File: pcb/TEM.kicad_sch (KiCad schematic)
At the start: 23 parts, among them J1 Conn_01x04_Pin, SW1 SW_Wuerth_450301014042, U1 AT24CM02-SSHM, U2 AT24CM02-SSHM

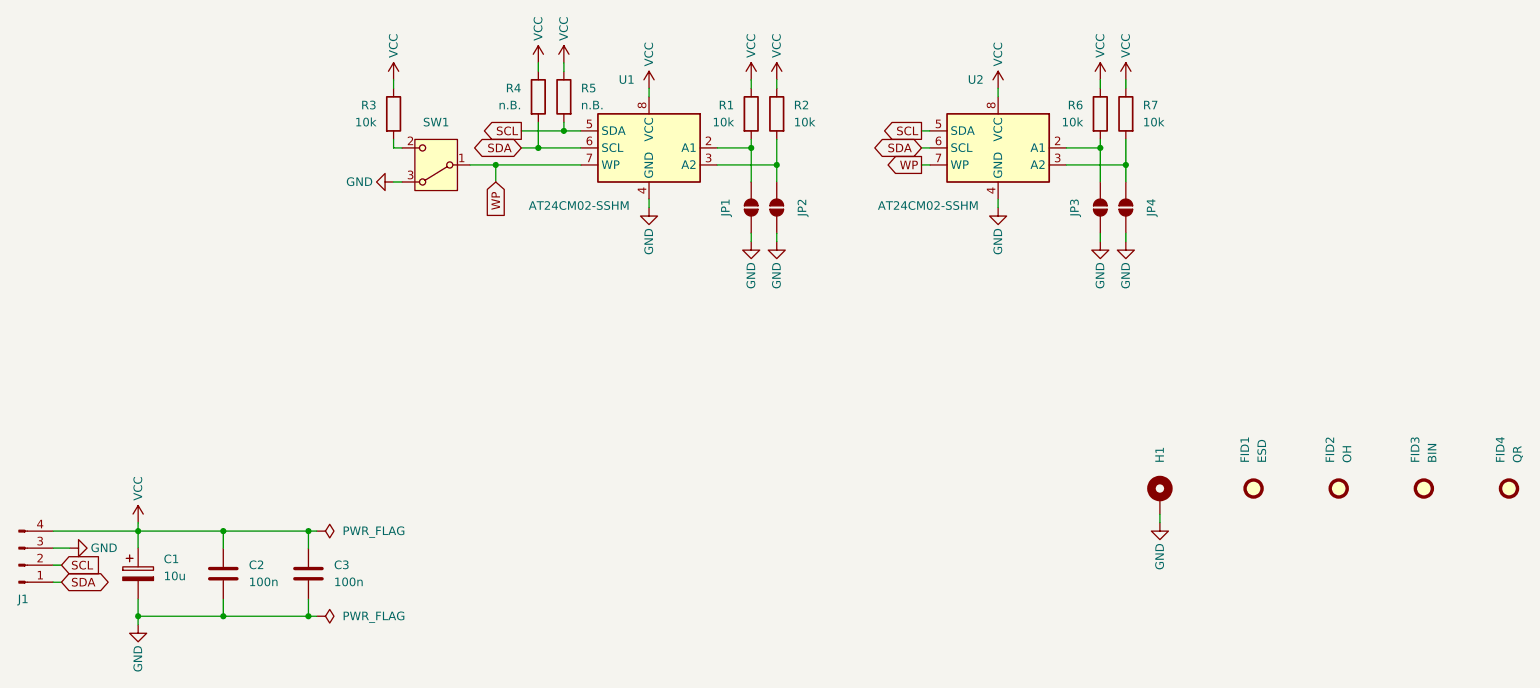
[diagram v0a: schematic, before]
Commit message: Swapped SCL/SDA
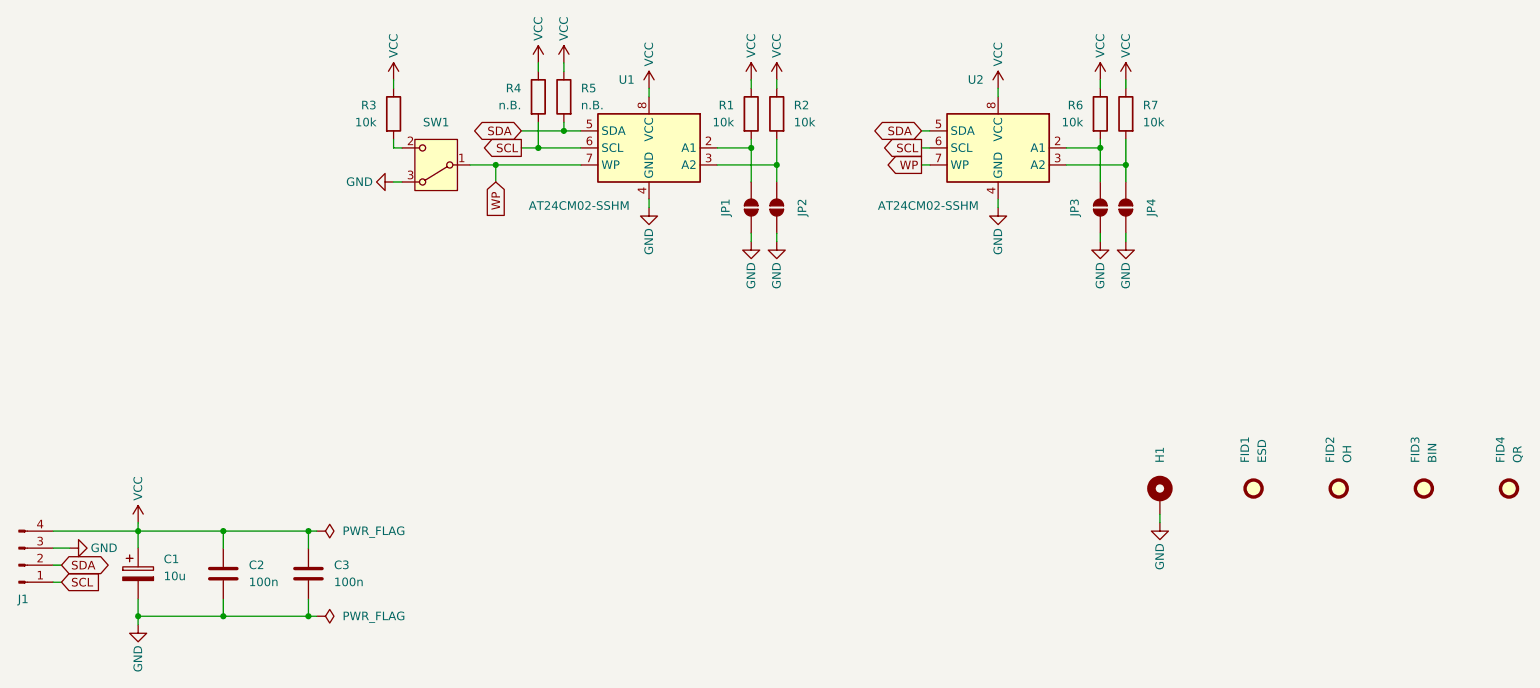
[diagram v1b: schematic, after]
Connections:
- net SCL: now also J1.1 (Pin_1), R4.2, U1.6 (SCL), U2.6 (SCL); no longer J1.2 (Pin_2), R5.2, U1.5 (SDA), U2.5 (SDA)
- net SDA: now also J1.2 (Pin_2), R5.2, U1.5 (SDA), U2.5 (SDA); no longer J1.1 (Pin_1), R4.2, U1.6 (SCL), U2.6 (SCL)
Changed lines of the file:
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@@
 	(global_label "SCL"
 		(shape output)
-		(at 167.64 99.06 180)
+		(at 167.64 101.6 180)
 		(fields_autoplaced yes)
 		(effects
@@
 		)
 		(property "Intersheetrefs" "${INTERSHEET_REFS}"
-			(at 161.1472 99.06 0)
+			(at 161.1472 101.6 0)
 			(effects
 				(font
@@
 	(global_label "SDA"
 		(shape bidirectional)
-		(at 107.95 101.6 180)
+		(at 107.95 99.06 180)
 		(fields_autoplaced yes)
 		(effects
@@
 		)
 		(property "Intersheetrefs" "${INTERSHEET_REFS}"
-			(at 100.2854 101.6 0)
+			(at 100.2854 99.06 0)
 			(effects
 				(font
@@
 	(global_label "SCL"
 		(shape input)
-		(at 39.37 163.83 0)
+		(at 39.37 166.37 0)
 		(fields_autoplaced yes)
 		(effects
@@
 		)
 		(property "Intersheetrefs" "${INTERSHEET_REFS}"
-			(at 45.8628 163.83 0)
+			(at 45.8628 166.37 0)
 			(effects
 				(font
@@
 	(global_label "SDA"
 		(shape bidirectional)
-		(at 39.37 166.37 0)
+		(at 39.37 163.83 0)
 		(fields_autoplaced yes)
 		(effects
@@
 		)
 		(property "Intersheetrefs" "${INTERSHEET_REFS}"
-			(at 47.0346 166.37 0)
+			(at 47.0346 163.83 0)
 			(effects
 				(font
@@
 	(global_label "SDA"
 		(shape bidirectional)
-		(at 167.64 101.6 180)
+		(at 167.64 99.06 180)
 		(fields_autoplaced yes)
 		(effects
@@
 		)
 		(property "Intersheetrefs" "${INTERSHEET_REFS}"
-			(at 159.9754 101.6 0)
+			(at 159.9754 99.06 0)
 			(effects
 				(font
@@
 	(global_label "SCL"
 		(shape output)
-		(at 107.95 99.06 180)
+		(at 107.95 101.6 180)
 		(fields_autoplaced yes)
 		(effects
@@
 		)
 		(property "Intersheetrefs" "${INTERSHEET_REFS}"
-			(at 101.4572 99.06 0)
+			(at 101.4572 101.6 0)
 			(effects
 				(font

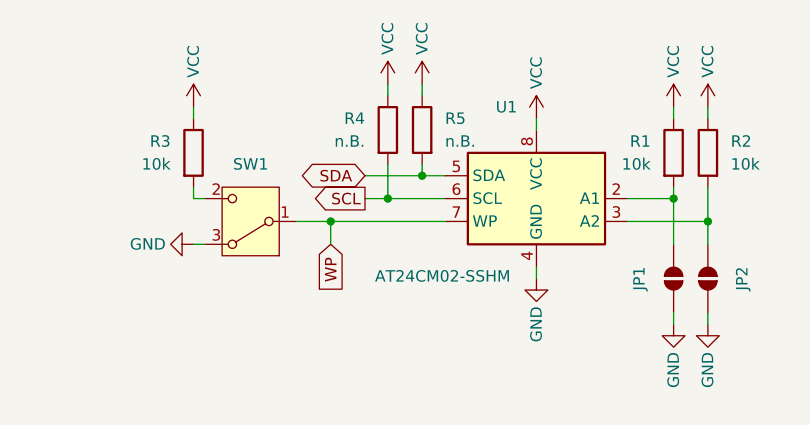
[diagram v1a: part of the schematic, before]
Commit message: Adapt vendors on partlist
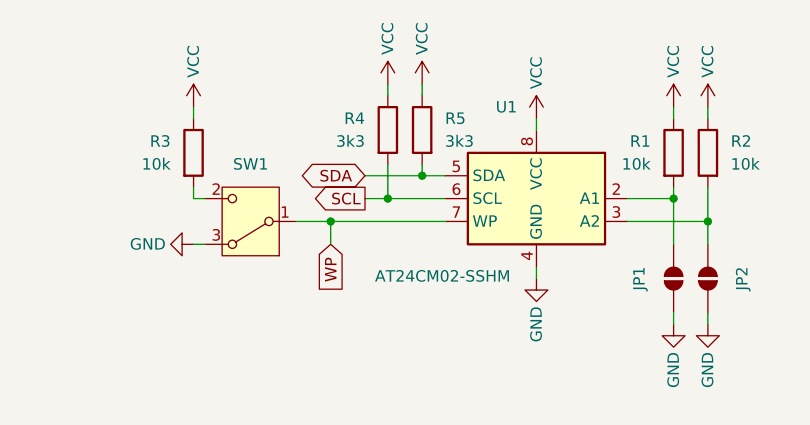
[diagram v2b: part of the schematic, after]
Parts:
- C1: Vendor (none) -> HTL; VendorId (none) -> 100140; now left out of the parts list
- C2, C3: Vendor (none) -> HTL; VendorId (none) -> 100128; now left out of the parts list
- FID1, FID2, FID3, FID4: now left out of the parts list
- R1, R2, R3, R6, R7: Vendor (none) -> HTL; VendorId (none) -> 102967
- R4, R5: value n.B. -> 3k3; Vendor (none) -> HTL; VendorId (none) -> 102959
- U1, U2: Vendor (none) -> HTL; VendorId (none) -> 103616
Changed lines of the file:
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@@
 		(unit 1)
 		(exclude_from_sim no)
-		(in_bom yes)
+		(in_bom no)
 		(on_board yes)
 		(dnp no)
@@
 		(unit 1)
 		(exclude_from_sim no)
-		(in_bom yes)
+		(in_bom no)
 		(on_board yes)
 		(dnp no)
@@
 			)
 		)
+		(property "Vendor" "HTL"
+			(at 63.5 165.1 0)
+			(effects
+				(font
+					(size 1.27 1.27)
+				)
+				(hide yes)
+			)
+		)
+		(property "VendorId" "100128"
+			(at 63.5 165.1 0)
+			(effects
+				(font
+					(size 1.27 1.27)
+				)
+				(hide yes)
+			)
+		)
 		(pin "1"
 		)
@@
 			)
 		)
-		(property "Value" "n.B."
+		(property "Value" "3k3"
 			(at 116.84 95.2499 0)
 			(effects
@@
 			)
 		)
+		(property "Vendor" "HTL"
+			(at 114.3 93.98 0)
+			(effects
+				(font
+					(size 1.27 1.27)
+				)
+				(hide yes)
+			)
+		)
+		(property "VendorId" "102959"
+			(at 114.3 93.98 0)
+			(effects
+				(font
+					(size 1.27 1.27)
+				)
+				(hide yes)
+			)
+		)
 		(pin "1"
 		)
@@
 		)
 		(property "Description" "Resistor"
+			(at 142.24 96.52 0)
+			(effects
+				(font
+					(size 1.27 1.27)
+				)
+				(hide yes)
+			)
+		)
+		(property "Vendor" "HTL"
+			(at 142.24 96.52 0)
+			(effects
+				(font
+					(size 1.27 1.27)
+				)
+				(hide yes)
+			)
+		)
+		(property "VendorId" "102967"
 			(at 142.24 96.52 0)
 			(effects
@@
 			)
 		)
+		(property "Vendor" "HTL"
+			(at 146.05 96.52 0)
+			(effects
+				(font
+					(size 1.27 1.27)
+				)
+				(hide yes)
+			)
+		)
+		(property "VendorId" "102967"
+			(at 146.05 96.52 0)
+			(effects
+				(font
+					(size 1.27 1.27)
+				)
+				(hide yes)
+			)
+		)
 		(pin "1"
 		)
@@
 			)
 		)
-		(property "Value" "n.B."
+		(property "Value" "3k3"
 			(at 107.95 95.2499 0)
 			(effects
@@
 			)
 		)
+		(property "Vendor" "HTL"
+			(at 110.49 93.98 0)
+			(effects
+				(font
+					(size 1.27 1.27)
+				)
+				(hide yes)
+			)
+		)
+		(property "VendorId" "102959"
+			(at 110.49 93.98 0)
+			(effects
+				(font
+					(size 1.27 1.27)
+				)
+				(hide yes)
+			)
+		)
 		(pin "1"
 		)
@@
 			)
 		)
+		(property "Vendor" "HTL"
+			(at 88.9 96.52 0)
+			(effects
+				(font
+					(size 1.27 1.27)
+				)
+				(hide yes)
+			)
+		)
+		(property "VendorId" "102967"
+			(at 88.9 96.52 0)
+			(effects
+				(font
+					(size 1.27 1.27)
+				)
+				(hide yes)
+			)
+		)
 		(pin "1"
 		)
@@
 		(unit 1)
 		(exclude_from_sim no)
-		(in_bom yes)
+		(in_bom no)
 		(on_board yes)
 		(dnp no)
@@
 			)
 		)
+		(property "Vendor" "HTL"
+			(at 50.8 165.1 0)
+			(effects
+				(font
+					(size 1.27 1.27)
+				)
+				(hide yes)
+			)
+		)
+		(property "VendorId" "100140"
+			(at 50.8 165.1 0)
+			(effects
+				(font
+					(size 1.27 1.27)
+				)
+				(hide yes)
+			)
+		)
 		(pin "1"
 		)
@@
 			)
 		)
+		(property "Vendor" "HTL"
+			(at 198.12 96.52 0)
+			(effects
+				(font
+					(size 1.27 1.27)
+				)
+				(hide yes)
+			)
+		)
+		(property "VendorId" "102967"
+			(at 198.12 96.52 0)
+			(effects
+				(font
+					(size 1.27 1.27)
+				)
+				(hide yes)
+			)
+		)
 		(pin "1"
 		)
@@
 		)
 		(property "Description" "Resistor"
+			(at 194.31 96.52 0)
+			(effects
+				(font
+					(size 1.27 1.27)
+				)
+				(hide yes)
+			)
+		)
+		(property "Vendor" "HTL"
+			(at 194.31 96.52 0)
+			(effects
+				(font
+					(size 1.27 1.27)
+				)
+				(hide yes)
+			)
+		)
+		(property "VendorId" "102967"
 			(at 194.31 96.52 0)
 			(effects
@@
 		(unit 1)
 		(exclude_from_sim no)
-		(in_bom yes)
+		(in_bom no)
 		(on_board yes)
 		(dnp no)
@@
 		(unit 1)
 		(exclude_from_sim no)
-		(in_bom yes)
+		(in_bom no)
 		(on_board yes)
 		(dnp no)
@@
 			)
 		)
+		(property "Vendor" "HTL"
+			(at 179.07 101.6 0)
+			(effects
+				(font
+					(size 1.27 1.27)
+				)
+				(hide yes)
+			)
+		)
+		(property "VendorId" "103616"
+			(at 179.07 101.6 0)
+			(effects
+				(font
+					(size 1.27 1.27)
+				)
+				(hide yes)
+			)
+		)
 		(pin "8"
 		)
@@
 		(unit 1)
 		(exclude_from_sim no)
-		(in_bom yes)
+		(in_bom no)
 		(on_board yes)
 		(dnp no)
@@
 			)
 		)
+		(property "Vendor" "HTL"
+			(at 127 101.6 0)
+			(effects
+				(font
+					(size 1.27 1.27)
+				)
+				(hide yes)
+			)
+		)
+		(property "VendorId" "103616"
+			(at 127 101.6 0)
+			(effects
+				(font
+					(size 1.27 1.27)
+				)
+				(hide yes)
+			)
+		)
 		(pin "8"
 		)
@@
 		(unit 1)
 		(exclude_from_sim no)
-		(in_bom yes)
+		(in_bom no)
 		(on_board yes)
 		(dnp no)
@@
 			(at 76.2 165.1 0)
 			(effects
+				(font
+					(size 1.27 1.27)
+				)
+				(hide yes)
+			)
+		)
+		(property "Vendor" "HTL"
+			(at 76.2 165.1 0)
+			(effects
+				(font
+					(size 1.27 1.27)
+				)
+				(hide yes)
+			)
+		)
+		(property "VendorId" "100128"
+			(at 76.2 165.1 0)
+			(effects

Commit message: Add vendor id to partlist
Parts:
- J1: Vendor (none) -> HTL; VendorId (none) -> 101523
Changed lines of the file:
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@@
+			)
+		)
+		(property "Vendor" "HTL"
+			(at 33.02 163.83 0)
+			(effects
+				(font
+					(size 1.27 1.27)
+				)
+				(hide yes)
+			)
+		)
+		(property "VendorId" "101523"
+			(at 33.02 163.83 0)
+			(effects
+				(font
+					(size 1.27 1.27)
+				)
+				(hide yes)
 			)
 		)

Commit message: Remove exclude from bom
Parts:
- C1, C2, C3: now in the parts list
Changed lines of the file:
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@@
 		(unit 1)
 		(exclude_from_sim no)
-		(in_bom no)
+		(in_bom yes)
 		(on_board yes)
 		(dnp no)
@@
 		(unit 1)
 		(exclude_from_sim no)
-		(in_bom no)
+		(in_bom yes)
 		(on_board yes)
 		(dnp no)
@@
 		(unit 1)
 		(exclude_from_sim no)
-		(in_bom no)
-		(on_board yes)
-		(dnp no)
+		(in_bom yes)
+		(on_board yes)
+		(dnp no)

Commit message: Add missing vendor(id)
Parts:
- H1: Vendor (none) -> HTL; VendorId (none) -> 100968, 101210; now in the parts list
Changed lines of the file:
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@@
 		(unit 1)
 		(exclude_from_sim no)
-		(in_bom no)
+		(in_bom yes)
 		(on_board yes)
 		(dnp no)
@@
 			(effects
 				(font
+					(size 1.27 1.27)
+				)
+				(hide yes)
+			)
+		)
+		(property "Vendor" "HTL"
+			(at 203.2 153.67 90)
+			(effects
+				(font
+					(size 1.27 1.27)
+				)
+				(hide yes)
+			)
+		)
+		(property "VendorId" "100968, 101210"
+			(at 203.2 153.67 90)
+			(effects
+				(font

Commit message: Adapt vendor(id)
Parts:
- SW1: Vendor DigiKey -> HTL; VendorId 2223-MSS-102545-28A-D-ND -> 103663
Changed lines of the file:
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@@
 			)
 		)
-		(property "Vendor" "DigiKey"
+		(property "Vendor" "HTL"
 			(at 95.25 104.14 0)
 			(effects
@@
 			)
 		)
-		(property "VendorId" "2223-MSS-102545-28A-D-ND"
+		(property "VendorId" "103663"
 			(at 95.25 104.14 0)
 			(effects
